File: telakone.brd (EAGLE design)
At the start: 100 x 100 mm, 171 parts, among them X10 MPT0.5/8-2.54, X11 MPT0.5/8-2.54, X2 MPT0.5/8-2.54, X3 MPT0.5/8-2.54, X4 PIIKKIRIMA-2, X5 PIIKKIRIMA-5, X7 U.FL-R-SMT-1, X8 MPT0.5/8-2.54, X9 629105136821

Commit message: placement, all on board
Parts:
- added C48, C49, C52: (no value), omat_ic_2:C0603
- added Y1, Y2, Y3, Y4: PTH2.6-5.5SQ, EKE:PTH-2.6-5.5SQ
- moved V27 156.0 mm to (12.7, 27.9), turned to 270 degrees
- moved R59 139.4 mm to (29.2, 19.1), turned to 270 degrees
- moved R46 139.3 mm to (17.8, 35.6), turned to 180 degrees
- moved V23 138.2 mm to (11.4, 17.8), turned to 270 degrees
- moved R45 135.0 mm to (21.6, 35.6), turned to 180 degrees
- moved R58 129.7 mm to (17.8, 17.8), turned to 90 degrees
- moved D2 122.5 mm to (24.1, 17.8), turned to 180 degrees
- moved R56 121.5 mm to (16.5, 31.8), turned to 180 degrees
- moved R57 117.8 mm to (16.5, 24.1), turned to 180 degrees
- moved N2 116.8 mm to (78.7, 68.6), turned to 180 degrees
- moved C46 114.2 mm to (78.7, 66.0)
- moved R54 113.4 mm to (12.7, 31.8), turned to 180 degrees
- moved R55 109.6 mm to (12.7, 24.1), turned to 180 degrees
- moved R53 104.8 mm to (14.0, 52.1)
- moved R52 101.6 mm to (14.0, 54.6)
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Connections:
- net +3V3: now also C48.1, C49.1, C52.1
- net GND: now also C48.2, C49.2, C52.2

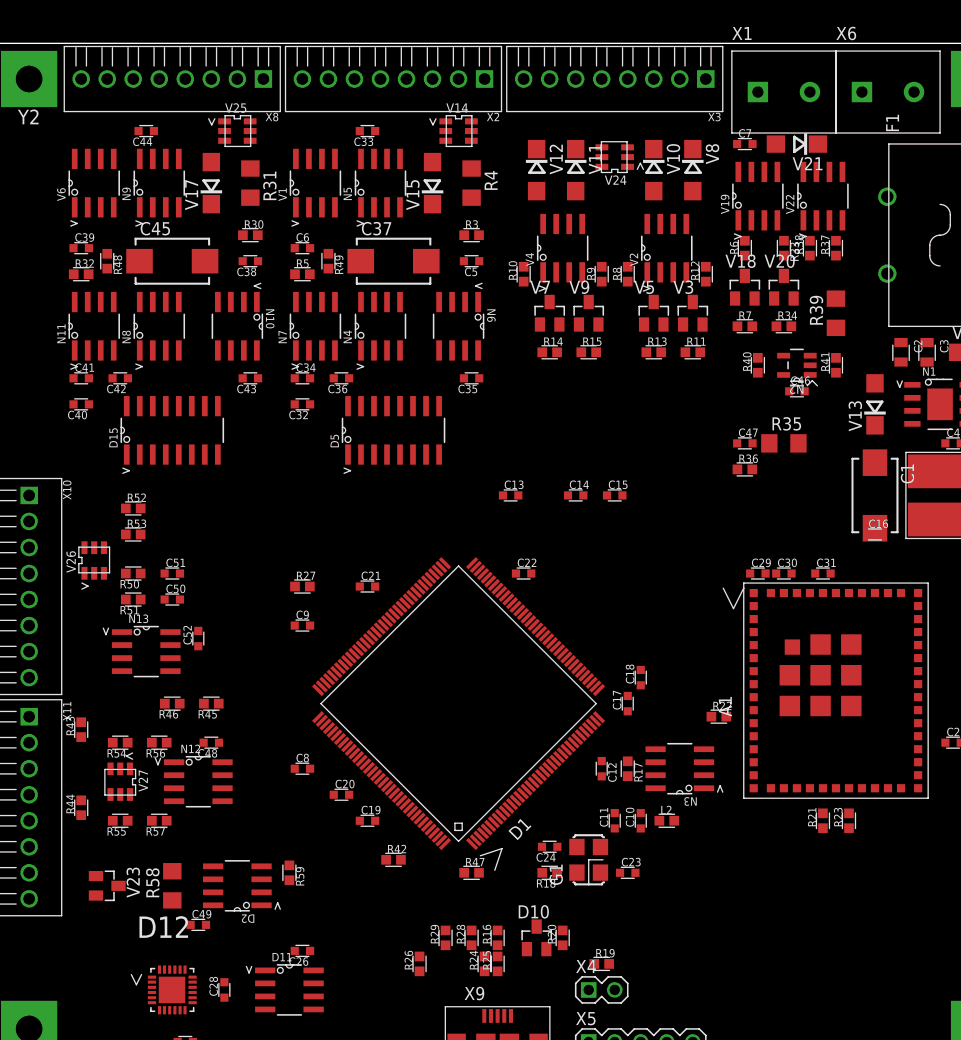
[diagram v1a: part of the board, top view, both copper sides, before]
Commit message: isolation groups routed
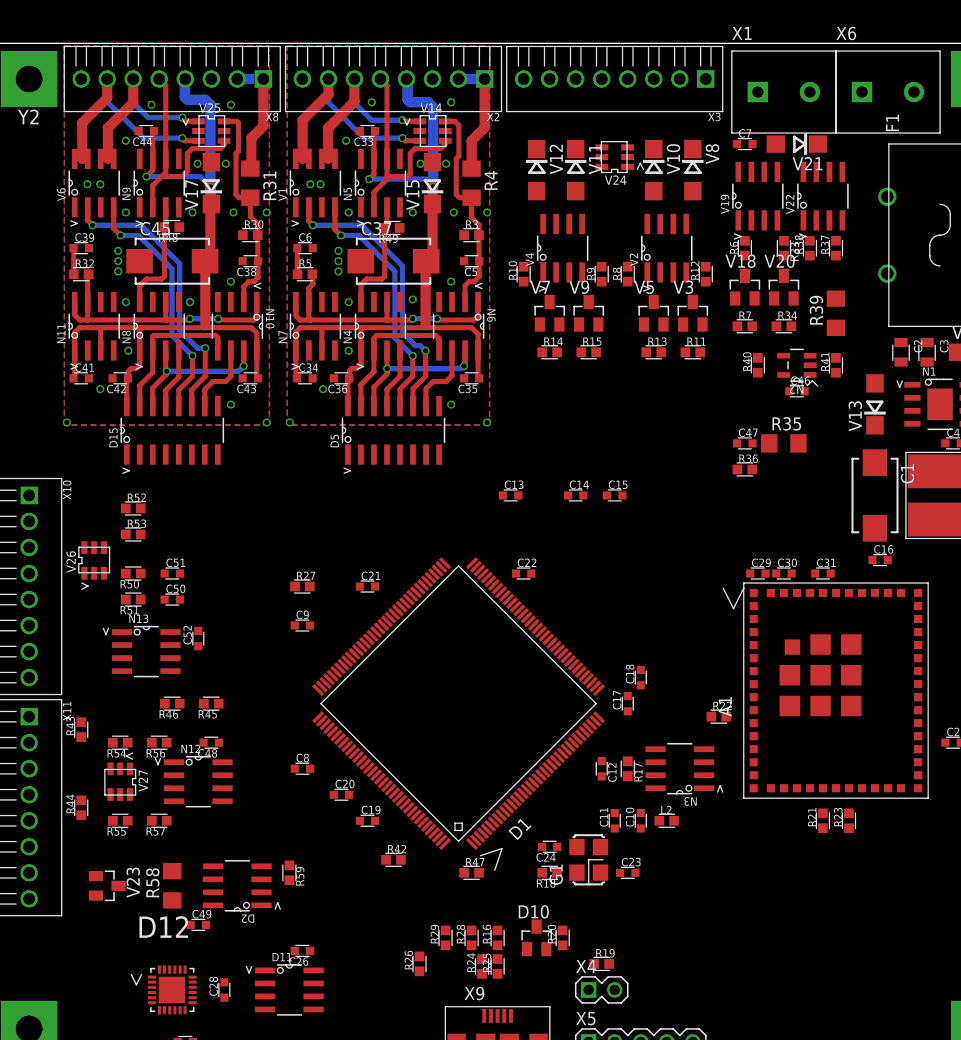
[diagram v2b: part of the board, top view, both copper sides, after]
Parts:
- removed C32, C40: 100n, omat_ic_2:C0603
- moved R48 7.13 mm to (17.7, 82.1), turned to 180 degrees
- moved R49 7.01 mm to (39.2, 82.0), turned to 180 degrees
- moved C16 2.55 mm to (86.9, 49.6)
- moved V14 2.54 mm to (43.2, 91.4)
- moved V25 2.54 mm to (21.6, 91.4)
- moved R24 0.35 mm to (48.0, 9.91)
- moved C34 0.25 mm to (30.7, 67.3)
- moved C6 0.25 mm to (30.7, 80.0)
- moved R25 0.25 mm to (49.5, 9.91)
- moved R5 0.25 mm to (30.7, 77.5)
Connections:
- net BRAKE_OD_1: now also V14.1; no longer V14.3
- net BRAKE_OD_2: now also V25.1; no longer V25.3
- net REVERSE_OD_1: now also V14.3; no longer V14.1
- net REVERSE_OD_2: now also V25.3; no longer V25.1
- net V+1: no longer C32.1
- net V+2: no longer C40.1
- net V-1: no longer C32.2
- net V-2: no longer C40.2
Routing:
- net V+2: track 0.00 -> 77.9 mm, vias 0 -> 2
- net V+1: track 0.00 -> 76.5 mm, vias 0 -> 2
- net REVERSE_2: track 0.00 -> 27.9 mm, vias 0 -> 2
- net REVERSE_1: track 0.00 -> 27.7 mm, vias 0 -> 2
- net VREF25_1: track 0.00 -> 27.4 mm, vias 0 -> 2
- net VREF25_2: track 0.00 -> 27.2 mm, vias 0 -> 2
- net BRAKE_2: track 0.00 -> 24.2 mm, vias 0 -> 2
- net BRAKE_1: track 0.00 -> 24.1 mm, vias 0 -> 2
- net REVERSE_OD_2: track 0.00 -> 22.9 mm, vias 0 -> 1
- net REVERSE_OD_1: track 0.00 -> 22.9 mm, vias 0 -> 1
- net THROTTLE_BUFFERED_2: track 0.00 -> 22.0 mm
- net THROTTLE_BUFFERED_1: track 0.00 -> 21.8 mm
- net AIN_2: track 0.00 -> 21.5 mm
- net AIN_1: track 0.00 -> 21.3 mm
- net BRAKE_OD_1: track 0.00 -> 19.6 mm, vias 0 -> 1
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- added copper zone on layer 1, net V-1
- added copper zone on layer 16, net V-1
- added copper zone on layer 1, net V-2
- added copper zone on layer 16, net V-2

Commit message: work commit, routing in progress
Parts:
- added C32, C40, C53: (no value), omat_ic_2:C0805
- added V28: WURTH 82402304, omat_ic_2:SOT23-6
- moved C51 24.1 mm to (17.0, 24.2)
- moved R51 23.3 mm to (14.0, 22.4)
- moved R50 23.3 mm to (14.0, 24.9)
- moved N13 23.1 mm to (15.5, 17.6)
- moved C52 22.9 mm to (20.0, 19.0)
- moved C50 22.7 mm to (17.0, 23.0)
- moved C48 21.6 mm to (22.1, 53.3)
- moved C49 21.6 mm to (20.3, 35.6)
- moved R54 21.6 mm to (12.7, 53.3)
- moved R56 21.6 mm to (16.5, 53.3)
- moved X10 21.6 mm to (3.81, 34.3)
- moved X11 21.6 mm to (3.81, 55.9)
- moved N12 21.6 mm to (20.3, 49.5)
- moved R55 21.6 mm to (12.7, 45.7)
- moved R57 21.6 mm to (16.5, 45.7)
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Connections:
- net N$33 renamed PA11-USBD-
- net N$36 renamed PA12-USBD+
- net N$37 renamed USBD+
- net N$38 renamed USBD-
- net N$39 renamed PA9-USBVBUS
- net N$40 renamed USBVBUS
- net N$41 renamed PA10-USBID-PULLUP
- net +12V: now also C32.1, C40.1, C53.1
- net BUTTON1: now also V26.3; no longer V26.1
- net BUTTON2: now also V26.4; no longer V26.3
- net GND: now also C32.2, C40.2, C53.2, V28.2, V28.5, X6.1, Y1.1, Y2.1, Y3.1, Y4.1; no longer X6.2
- net N$8: now also X6.2; no longer X6.1
- net POT_IN_1: now also V28.3; no longer V26.4
- net POT_IN_2: now also V28.6; no longer V26.6
- net VREF25BUF: now also V28.4; no longer V27.1
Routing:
- net +12V: track 0.00 -> 211.8 mm, vias 0 -> 9
- net VREF25BUF: track 0.00 -> 65.7 mm
- net N$7: track 0.00 -> 32.4 mm
- net +3V3: track 0.00 -> 27.2 mm
- net NERT4: track 0.00 -> 26.7 mm
- net N$1: track 0.00 -> 25.5 mm
- net N$8: track 0.00 -> 23.9 mm
- net ACCRTXLO: track 0.00 -> 19.1 mm
- net ACCRTXHI: track 0.00 -> 19.1 mm
- net NERT5: track 0.00 -> 18.4 mm
- net N$17: track 0.00 -> 15.4 mm
- net N$21: track 0.00 -> 15.3 mm
- net BUTTON2: track 0.00 -> 15.1 mm
- net BUTTON1: track 0.00 -> 14.7 mm
- net MOTOR_L2: track 0.00 -> 14.4 mm
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- added copper zone on layer 1, net GND
- added copper zone on layer 16, net GND

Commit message: work commit, routing in progress, less than 100 to go :beer:
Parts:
- removed R18, R27: (no value), omat_ic_2:R0603
- removed R24, R25: 22, omat_ic_2:R0603
- removed R26: 1k, omat_ic_2:R0603
- removed X9: 629105136821, omat_ic_2:629105136821
- added C54: 2u2, omat_ic_2:C0603
- added C55: 100n, omat_ic_2:C0603
- added C56, C57: (no value), omat_ic_2:C0603
- added L3: IND0603, omat_ic_2:R0603
- moved C16 44.8 mm to (51.3, 22.4), turned to 45 degrees
- moved X5 34.7 mm to (27.1, 17.4)
- moved C14 33.3 mm to (29.8, 36.8), turned to 135 degrees
- moved C15 31.4 mm to (54.0, 25.3), turned to 225 degrees
- moved R20 29.9 mm to (58.4, 42.5), turned to 225 degrees
- moved C18 28.6 mm to (35.4, 43.7), turned to 45 degrees
- moved R19 22.9 mm to (39.9, 21.6), turned to 45 degrees
- moved X4 21.1 mm to (39.8, 17.4)
- moved C9 20.1 mm to (49.4, 49.9), turned to 315 degrees
- moved C13 19.8 mm to (61.0, 38.9), turned to 315 degrees
- moved R47 14.9 mm to (32.1, 20.3), turned to 90 degrees
- moved R29 11.8 mm to (32.6, 13.6), turned to 180 degrees
- moved R28 10.3 mm to (36.7, 13.6), turned to 0 degrees
- moved C17 9.80 mm to (56.4, 43.4), turned to 315 degrees
- moved R42 9.78 mm to (29.6, 20.3), turned to 90 degrees
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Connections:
- net N$26 renamed OSCIN
- removed net DSPICLK: D15.3
- removed net N$27: D1.24, R18.2
- removed net N$28: C24.1, G1.3, R18.1
- removed net PA10-USBID-PULLUP: D1.102, R27.2
- removed net PA11-USBD-: D1.103, R24.2
- removed net PA12-USBD+: D1.104, R25.2
- removed net PA9-USBVBUS: D1.101, R26.2
- removed net USBD+: R25.1, X9.3
- removed net USBD-: R24.1, X9.2
- removed net USBVBUS: R26.1, X9.1
- new net OSCOUT: C24.1, D1.24, G1.3
- new net VDDAREF: C54.1, C55.1, L3.1, N3.1, N3.3
- net +3V3: now also C56.1, C57.1, L3.2; no longer N3.1, N3.3, R27.1
- net D2SPICLK: now also D15.3
- net GND: now also C54.2, C55.2, C56.2, C57.2, X5.4; no longer X5.5, X9.5, X9.Z1, X9.Z2, X9.Z3, X9.Z4
- net RESETL: now also X5.5; no longer X5.4
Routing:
- net MOTOR_H2: track 2.81 -> 77.9 mm, vias 0 -> 2
- net MOTOR_H1: track 2.80 -> 76.7 mm, vias 0 -> 2
- net VREF25: track 8.21 -> 75.6 mm, vias 0 -> 2
- net OUT1: track 2.80 -> 66.0 mm, vias 0 -> 2
- net OUT2: track 2.80 -> 62.0 mm, vias 0 -> 2
- net OUT3: track 2.55 -> 55.7 mm, vias 0 -> 2
- net OUT4: track 2.55 -> 52.4 mm, vias 0 -> 2
- net RESETL: track 0.00 -> 47.8 mm
- net I2C1SCL: track 0.00 -> 41.3 mm
- net BUTTON2: track 15.1 -> 55.7 mm, vias 0 -> 2
- net D2SPIMOSI: track 0.00 -> 39.8 mm, vias 0 -> 2
- net POT2: track 5.42 -> 44.9 mm, vias 0 -> 2
- net MEAS12V: track 0.00 -> 39.5 mm
- net D2SPICLK: track 0.00 -> 38.8 mm, vias 0 -> 2
- net POT1: track 4.92 -> 43.6 mm, vias 0 -> 2
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
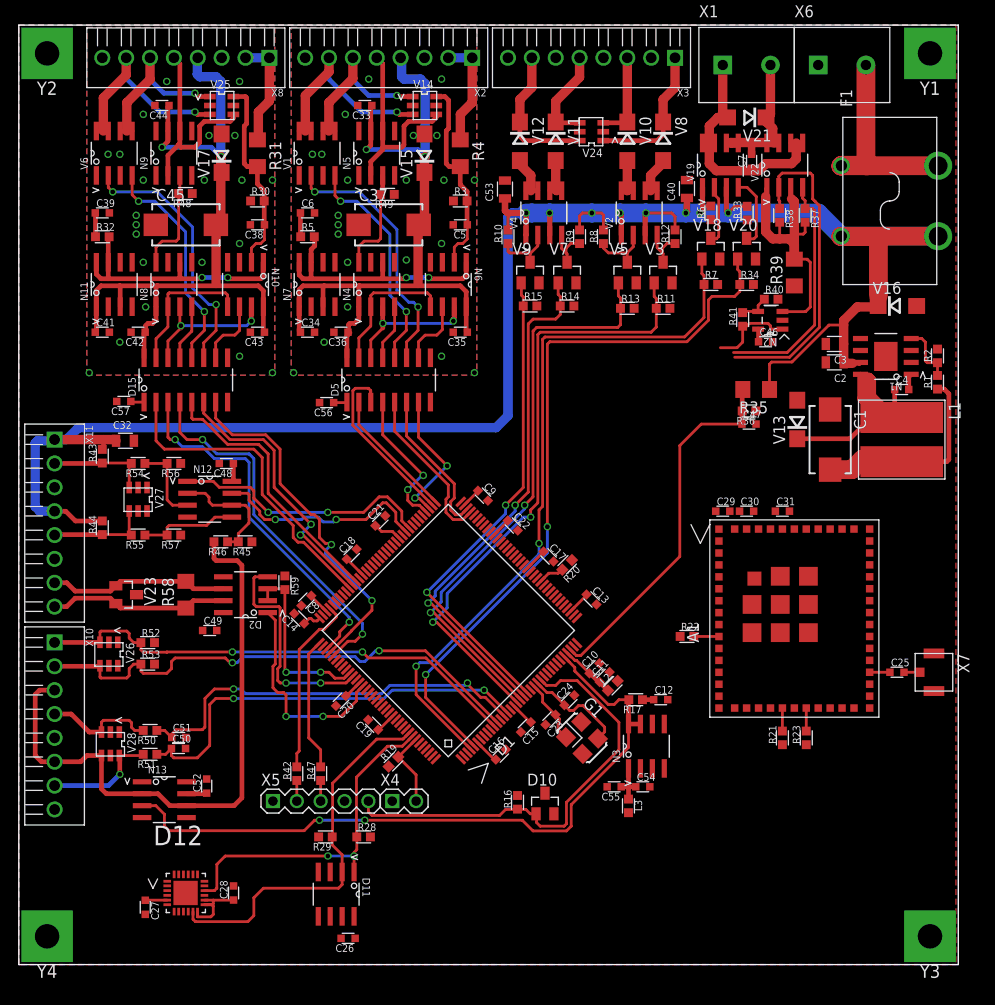
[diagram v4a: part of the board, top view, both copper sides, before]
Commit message: fully routed
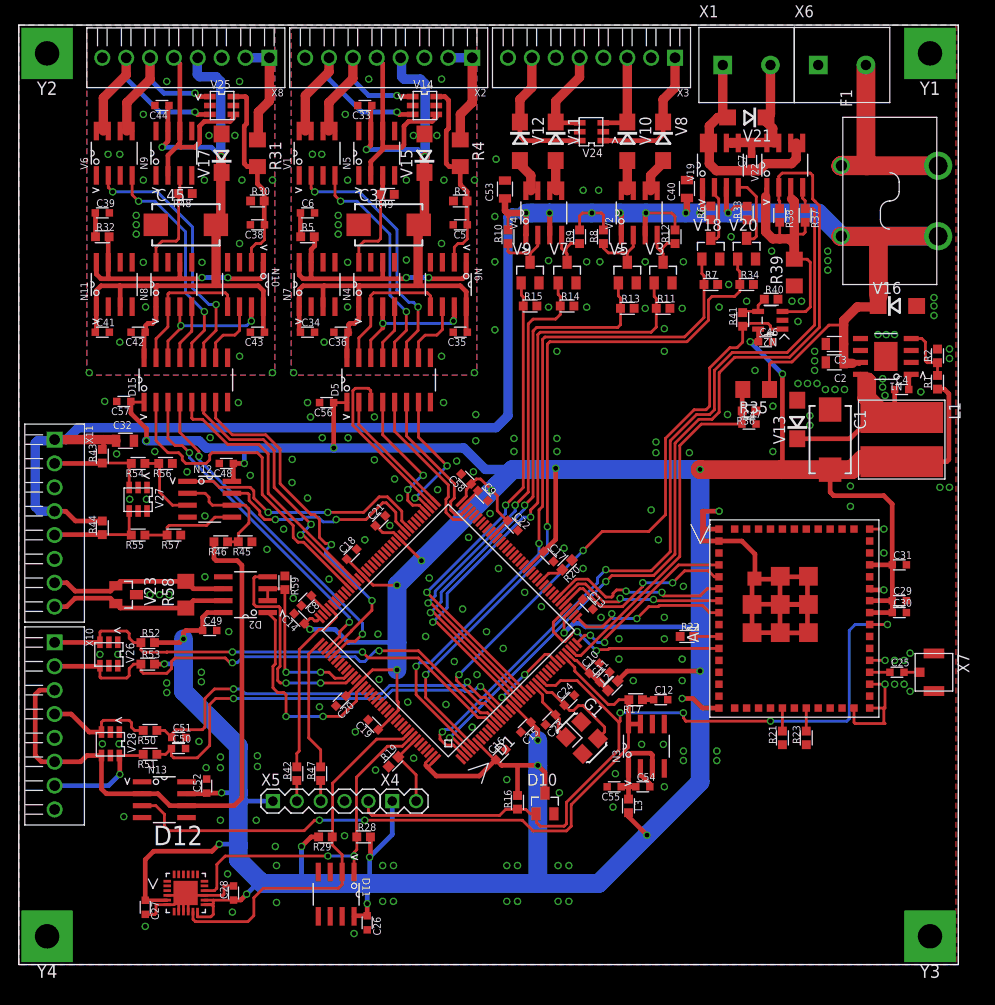
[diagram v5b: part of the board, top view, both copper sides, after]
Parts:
- added C58: 100n, omat_ic_2:C0603
- moved C29 21.1 mm to (93.7, 38.7)
- moved C30 19.5 mm to (93.7, 37.5)
- moved C31 13.7 mm to (93.7, 42.5)
- moved C26 2.62 mm to (37.1, 4.45), turned to 270 degrees
- moved R56 0.89 mm to (15.6, 53.3)
- moved C13 0.64 mm to (60.6, 38.4)
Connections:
- net +3V3: now also C58.1
- net GND: now also C58.2
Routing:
- net +3V3: track 65.5 -> 535.7 mm, vias 0 -> 27
- net GND: track 0.00 -> 98.5 mm, vias 0 -> 200
- net MOTOR_L1: track 25.6 -> 87.2 mm, vias 0 -> 2
- net MOTOR_L2: track 34.1 -> 93.3 mm, vias 0 -> 2
- net MOTOR_CURR: track 9.07 -> 65.6 mm, vias 0 -> 2
- net RESETL: track 47.8 -> 89.7 mm, vias 0 -> 4
- net CCIRQ: track 0.00 -> 22.6 mm, vias 0 -> 2
- net CCSPICLK: track 0.00 -> 20.1 mm, vias 0 -> 2
- net CCSPIMOSI: track 0.00 -> 20.0 mm, vias 0 -> 2
- net CCHIBL: track 0.00 -> 19.4 mm, vias 0 -> 2
- net CCSPIMISO: track 0.00 -> 18.8 mm, vias 0 -> 2
- net CCSPICSL: track 0.00 -> 17.6 mm, vias 0 -> 2
- net VDDAREF: track 4.81 -> 10.3 mm
- net D2SPICLK: track 38.8 -> 35.8 mm
- net D2SPIMOSI: track 39.8 -> 37.0 mm
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
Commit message: Layout finished
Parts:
- added H1: RED, omat_ic_2:CHIP-LED0603
- added H2, H3: GRN, omat_ic_2:CHIP-LED0603
- added R18, R24, R25: (no value), omat_ic_2:R0603
- added U$1: DAFUG, dafug:DAFUG
- added X9: PIIKKIRIMA-3, omat_ic_2:PIIKKIRIMA-3
- added Y5: PTH2.6-5.5SQ, EKE:PTH-2.6-5.5SQ
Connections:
- new net N$23: H2.C, R24.2
- new net N$25: H1.C, R18.2
- new net N$26: D1.139, H1.A
- new net N$27: D1.140, H2.A
- new net N$28: H3.C, R25.2
- new net USART1CTS: A1.P44, D1.103
- new net USART1RTS: A1.P51, D1.104
- new net USART1RX: A1.P46, D1.102
- new net USART1TX: A1.P47, D1.101
- new net USART3RX: D1.78, X9.2
- new net USART3TX: D1.77, X9.3
- net +3V3: now also H3.A
- net GND: now also R18.1, R24.1, R25.1, X9.1, Y5.1
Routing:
- net USART1CTS: track 0.00 -> 66.0 mm, vias 0 -> 2
- net USART1TX: track 0.00 -> 65.8 mm, vias 0 -> 2
- net USART1RX: track 0.00 -> 61.1 mm, vias 0 -> 2
- net USART1RTS: track 0.00 -> 56.7 mm, vias 0 -> 2
- net GND: track 98.5 -> 67.6 mm, vias 200 -> 229
- net N$33: track 0.00 -> 27.2 mm
- net N$27: track 0.00 -> 13.3 mm, vias 0 -> 2
- net N$26: track 0.00 -> 12.0 mm, vias 0 -> 2
- net USART3RX: track 0.00 -> 10.7 mm
- net USART3TX: track 0.00 -> 8.25 mm
- net +3V3: track 535.7 -> 542.5 mm, vias 27 -> 28
- net N$25: track 0.00 -> 1.58 mm
- net N$28: track 0.00 -> 1.53 mm
- net N$23: track 0.00 -> 1.53 mm
- net MOTOR_CURR: track 65.6 -> 64.2 mm
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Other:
- board text added: "ERR"
- board text added: "PWR"
- board text added: "RUN"
- board text added: "TELAKONE OHJAIN KIMMOLI 2016"
- board text added: "https://github.com/kimmoli/telakone-controller"
